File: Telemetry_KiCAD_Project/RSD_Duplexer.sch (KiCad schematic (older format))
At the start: 1 part

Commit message: Annotated Components
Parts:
- gave numbers to parts that had none: 1
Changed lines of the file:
@@
 $Descr A4 11693 8268
 encoding utf-8
-Sheet 5 8
+Sheet 2 8
 Title ""
 Date ""
@@
 $EndDescr
 $Comp
-L power:GND #PWR?
+L power:GND #PWR0102
 U 1 1 619F077A
 P 6250 4350
-F 0 "#PWR?" H 6250 4100 50  0001 C CNN
+F 0 "#PWR0102" H 6250 4100 50  0001 C CNN
 F 1 "GND" H 6255 4177 50  0000 C CNN
 F 2 "" H 6250 4350 50  0001 C CNN
@@
 $EndComp
 $Comp
-L power:GND #PWR?
+L power:GND #PWR0103
 U 1 1 619F08A7
 P 4350 4400
-F 0 "#PWR?" H 4350 4150 50  0001 C CNN
+F 0 "#PWR0103" H 4350 4150 50  0001 C CNN
 F 1 "GND" H 4355 4227 50  0000 C CNN
 F 2 "" H 4350 4400 50  0001 C CNN
@@
 	6250 4050 6250 3900
 $Comp
-L RDT_Custom_Symbols:RSD-897.500-942.500-1612-TR U?
+L RDT_Custom_Symbols:RSD-897.500-942.500-1612-TR U1
 U 1 1 619F0FB1
 P 5350 3650
-F 0 "U?" H 5350 3815 50  0000 C CNN
+F 0 "U1" H 5350 3815 50  0000 C CNN
 F 1 "RSD-897.500-942.500-1612-TR" H 5350 3724 50  0000 C CNN
 F 2 "" H 5350 3650 50  0001 C CNN

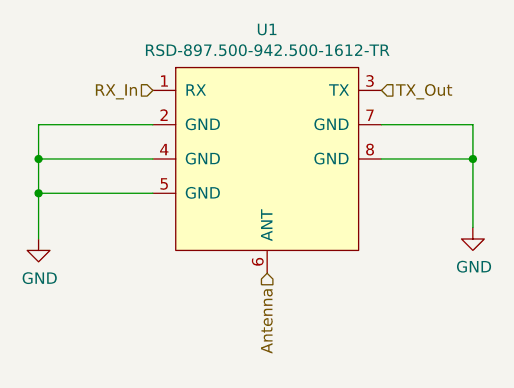
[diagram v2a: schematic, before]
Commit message: Corrected hierarchical pin directions, squashed bugs
There are still some warnings about pins being connected but not driven, don't know how to fix those at the moment
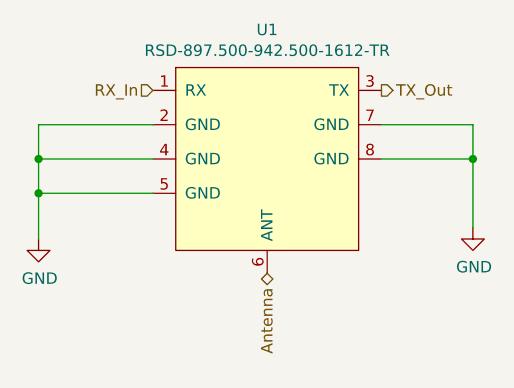
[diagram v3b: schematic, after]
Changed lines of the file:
@@
 	1    0    0    -1
 $EndComp
-Text HLabel 5850 3750 2    50   Input ~ 0
+Text HLabel 5850 3750 2    50   Output ~ 0
 TX_Out
 Text HLabel 4850 3750 0    50   Input ~ 0
 RX_In
-Text HLabel 5350 4550 3    50   Input ~ 0
+Text HLabel 5350 4550 3    50   BiDi ~ 0
 Antenna
 $EndSCHEMATC

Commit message: Added RSD Duplexer Footprint, rearranged RF matching networks
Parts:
- U1: footprint (none) -> RDT_Custom_Footprints:RSD-897.500-942.500-1612-TR
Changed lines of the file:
@@
 F 0 "U1" H 5350 3815 50  0000 C CNN
 F 1 "RSD-897.500-942.500-1612-TR" H 5350 3724 50  0000 C CNN
-F 2 "" H 5350 3650 50  0001 C CNN
+F 2 "RDT_Custom_Footprints:RSD-897.500-942.500-1612-TR" H 5350 3650 50  0001 C CNN
 F 3 "" H 5350 3650 50  0001 C CNN
 	1    5350 3650
